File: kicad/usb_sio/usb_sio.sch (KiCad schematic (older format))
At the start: 3 parts

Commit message: Update nrc2016 schema and PCB to use new library symbols
I've added proper schematic symbols for the pre-defined bus sockets to
stop confusion and error by just using the generic "library" socket
component and then relying on the net names to define the pins. Screwed
me once with the VCC and GND switch around, not going to happen again.
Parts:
- removed P?: CONN_01X40, symbol CONN_01X40
- removed U?: MCP2221A, symbol MCP2221A
- added BUS?: Z80_Bus, symbol Z80_Bus
- added C?: CP, symbol CP
- added C? (x2): C, symbol C
- added JP?: JUMPER3, symbol JUMPER3
- added R?: R, symbol R
- added U?: MCP2200, symbol MCP2200
- added U?: 68B50, symbol 68B50
- added U?: DIP_OSCILLATOR, symbol DIP_OSCILLATOR
- added Y?: Crystal, symbol Crystal
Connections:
- net labels added: A0, A6, A7, D0, D1, D2, D3, D4, D5, D6, D7, RX, TX, WR, ~CLK, ~INT, ~M1, ~WR
- net labels removed: ~RESET
- wire segments 8 -> 70
- no-connect marks 0 -> 21
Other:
- note added: "Oscillator Freq: 1.8432MHz\n\nProvides 115200 and 28800 baud without overclocking 68B50"

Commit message: More moving things around. Added sockets and pins symbols
Makes it easier for DRC and has hints for the right footprints already.
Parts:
- removed P?: CONN_01X02, symbol CONN_01X02
- added CON1: USB, symbol USB
- added P?: IO_BUS_PINS, symbol IO_BUS_PINS
- gave numbers to parts that had none: 10
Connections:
- wire segments 70 -> 67
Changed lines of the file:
@@
 $EndDescr
 $Comp
-L CONN_01X02 P?
-U 1 1 57B19EE3
-P 2450 2550
-F 0 "P?" H 2450 2700 50  0000 C CNN
-F 1 "CONN_01X02" V 2550 2550 50  0000 C CNN
-F 2 "" H 2450 2550 50  0000 C CNN
-F 3 "" H 2450 2550 50  0000 C CNN
-	1    2450 2550
-	-1   0    0    -1
-$EndComp
-$Comp
-L MCP2200 U?
+L MCP2200 U1
 U 1 1 57D39A59
 P 4750 2400
-F 0 "U?" H 4900 2450 60  0000 C CNN
+F 0 "U1" H 4900 2450 60  0000 C CNN
 F 1 "MCP2200" H 5350 2450 60  0000 C CNN
 F 2 "" H 4750 2600 60  0000 C CNN
@@
 	2650 2600 3700 2600
 $Comp
-L CP C?
+L CP C1
 U 1 1 57D39AA5
 P 2800 3150
-F 0 "C?" H 2825 3250 50  0000 L CNN
+F 0 "C1" H 2825 3250 50  0000 L CNN
 F 1 "CP" H 2825 3050 50  0000 L CNN
 F 2 "" H 2838 3000 50  0000 C CNN
@@
 	2800 3300 2800 3400
 $Comp
-L GND #PWR?
+L GND #PWR01
 U 1 1 57D39AF5
 P 2800 3400
-F 0 "#PWR?" H 2800 3150 50  0001 C CNN
+F 0 "#PWR01" H 2800 3150 50  0001 C CNN
 F 1 "GND" H 2800 3250 50  0000 C CNN
 F 2 "" H 2800 3400 50  0000 C CNN
@@
 $EndComp
 $Comp
-L Crystal Y?
+L Crystal Y1
 U 1 1 57D39BB8
 P 3750 4300
-F 0 "Y?" H 3750 4450 50  0000 C CNN
+F 0 "Y1" H 3750 4450 50  0000 C CNN
 F 1 "Crystal" H 3750 4150 50  0000 C CNN
 F 2 "" H 3750 4300 50  0000 C CNN
@@
 	3700 3600 3400 3600
 Wire Wire Line
-	3400 3600 3400 4300
-Wire Wire Line
-	3400 4300 3400 4500
+	3400 3600 3400 4500
 Wire Wire Line
 	3400 4300 3600 4300
@@
 	3900 4300 4100 4300
 Wire Wire Line
-	4100 3950 4100 4300
-Wire Wire Line
-	4100 4300 4100 4450
+	4100 3950 4100 4450
 Wire Wire Line
 	4100 3950 3600 3950
@@
 	3600 3700 3700 3700
 $Comp
-L C C?
+L C C2
 U 1 1 57D39C34
 P 3400 4650
-F 0 "C?" H 3425 4750 50  0000 L CNN
+F 0 "C2" H 3425 4750 50  0000 L CNN
 F 1 "C" H 3425 4550 50  0000 L CNN
 F 2 "" H 3438 4500 50  0000 C CNN
@@
 $EndComp
 $Comp
-L C C?
+L C C3
 U 1 1 57D39C64
 P 4100 4650
-F 0 "C?" H 4125 4750 50  0000 L CNN
+F 0 "C3" H 4125 4750 50  0000 L CNN
 F 1 "C" H 4125 4550 50  0000 L CNN
 F 2 "" H 4138 4500 50  0000 C CNN
@@
 	4100 4800 4100 4900
 $Comp
-L GND #PWR?
+L GND #PWR02
 U 1 1 57D39D01
 P 3400 4900
-F 0 "#PWR?" H 3400 4650 50  0001 C CNN
+F 0 "#PWR02" H 3400 4650 50  0001 C CNN
 F 1 "GND" H 3400 4750 50  0000 C CNN
 F 2 "" H 3400 4900 50  0000 C CNN
@@
 $EndComp
 $Comp
-L GND #PWR?
+L GND #PWR03
 U 1 1 57D39D28
 P 4100 4900
-F 0 "#PWR?" H 4100 4650 50  0001 C CNN
+F 0 "#PWR03" H 4100 4650 50  0001 C CNN
 F 1 "GND" H 4100 4750 50  0000 C CNN
 F 2 "" H 4100 4900 50  0000 C CNN
@@
 $EndComp
 $Comp
-L R R?
+L R R1
 U 1 1 57D39FA2
 P 3400 2050
-F 0 "R?" V 3480 2050 50  0000 C CNN
+F 0 "R1" V 3480 2050 50  0000 C CNN
 F 1 "R" V 3400 2050 50  0000 C CNN
 F 2 "" V 3330 2050 50  0000 C CNN
@@
 	3400 1900 3400 1800
 $Comp
-L VCC #PWR?
+L VCC #PWR04
 U 1 1 57D3A036
 P 3400 1800
-F 0 "#PWR?" H 3400 1650 50  0001 C CNN
+F 0 "#PWR04" H 3400 1650 50  0001 C CNN
 F 1 "VCC" H 3400 1950 50  0000 C CNN
 F 2 "" H 3400 1800 50  0000 C CNN
@@
 $EndComp
 $Comp
-L 68B50 U?
+L 68B50 U2
 U 1 1 57D3A94D
 P 5850 4800
-F 0 "U?" H 5950 6750 60  0000 C CNN
+F 0 "U2" H 5950 6750 60  0000 C CNN
 F 1 "68B50" H 6600 6750 60  0000 C CNN
 F 2 "" H 6150 5400 60  0000 C CNN
@@
 	5400 3800 5650 3800
 $Comp
-L DIP_OSCILLATOR U?
+L DIP_OSCILLATOR U3
 U 1 1 57D3CFC5
 P 4650 5500
-F 0 "U?" H 5000 5450 60  0000 C CNN
+F 0 "U3" H 5000 5450 60  0000 C CNN
 F 1 "DIP_OSCILLATOR" V 4600 5800 60  0000 C CNN
 F 2 "" H 4650 5500 60  0000 C CNN
@@
 	5200 5200 5600 5200
 Wire Wire Line
-	5400 4200 5400 4300
-Wire Wire Line
-	5400 4300 5400 4950
+	5400 4200 5400 4950
 Wire Wire Line
 	5400 4200 5650 4200
@@
 Connection ~ 5400 4300
 $Comp
-L VCC #PWR?
+L VCC #PWR05
 U 1 1 57D3D08C
 P 4850 4650
-F 0 "#PWR?" H 4850 4500 50  0001 C CNN
+F 0 "#PWR05" H 4850 4500 50  0001 C CNN
 F 1 "VCC" H 4850 4800 50  0000 C CNN
 F 2 "" H 4850 4650 50  0000 C CNN
@@
 $EndComp
 $Comp
-L GND #PWR?
+L GND #PWR06
 U 1 1 57D3D0B5
 P 4850 5750
-F 0 "#PWR?" H 4850 5500 50  0001 C CNN
+F 0 "#PWR06" H 4850 5500 50  0001 C CNN
 F 1 "GND" H 4850 5600 50  0000 C CNN
 F 2 "" H 4850 5750 50  0000 C CNN
@@
 	5150 4000 5150 4200
 $Comp
-L GND #PWR?
+L GND #PWR07
 U 1 1 57D3D18D
 P 5150 4200
-F 0 "#PWR?" H 5150 3950 50  0001 C CNN
+F 0 "#PWR07" H 5150 3950 50  0001 C CNN
 F 1 "GND" H 5150 4050 50  0000 C CNN
 F 2 "" H 5150 4200 50  0000 C CNN
@@
 	8500 4150 8600 4050
 Wire Bus Line
-	7350 3100 7350 3200
+	7350 3100 7350 5400
 Wire Bus Line
-	7350 3200 7350 3300
+	8500 5400 7350 5400
 Wire Bus Line
-	7350 3300 7350 3500
-Wire Bus Line
-	7350 3500 7350 3600
-Wire Bus Line
-	7350 3600 7350 3700
-Wire Bus Line
-	7350 3700 7350 3800
-Wire Bus Line
-	7350 3800 7350 3900
-Wire Bus Line
-	7350 3900 7350 4000
-Wire Bus Line
-	7350 4000 7350 4100
-Wire Bus Line
-	7350 4100 7350 4200
-Wire Bus Line
-	7350 4200 7350 4400
-Wire Bus Line
-	7350 4400 7350 4500
-Wire Bus Line
-	7350 4500 7350 4800
-Wire Bus Line
-	7350 4800 7350 5300
-Wire Bus Line
-	7350 5300 7350 5400
-Wire Bus Line
-	7350 5400 8500 5400
-Wire Bus Line
-	8500 5400 8500 4850
-Wire Bus Line
-	8500 4850 8500 4750
-Wire Bus Line
-	8500 4750 8500 4650
-Wire Bus Line
-	8500 4650 8500 4550
-Wire Bus Line
-	8500 4550 8500 4450
-Wire Bus Line
-	8500 4450 8500 4350
-Wire Bus Line
-	8500 4350 8500 4250
-Wire Bus Line
-	8500 4250 8500 4150
-Wire Bus Line
-	8500 4150 8500 3850
-Wire Bus Line
-	8500 3850 8500 3650
-Wire Bus Line
-	8500 3650 8500 3350
-Wire Bus Line
-	8500 3350 8500 3250
-Wire Bus Line
-	8500 3250 8500 2650
-Wire Bus Line
-	8500 2650 8500 2550
+	8500 2550 8500 5400
 Text Label 5600 3500 2    60   ~ 0
 TX
@@
 	9000 3550 8600 3550
 $Comp
-L Z80_Bus BUS?
+L Z80_Bus BUS1
 U 1 1 57D3DBDC
 P 9000 1450
-F 0 "BUS?" H 9350 1400 60  0000 C CNN
+F 0 "BUS1" H 9350 1400 60  0000 C CNN
 F 1 "Z80_Bus" V 9550 1100 60  0000 C CNN
 F 2 "" H 9000 1450 60  0000 C CNN
@@
 NoConn ~ 9000 3850
 $Comp
-L JUMPER3 JP?
+L JUMPER3 JP1
 U 1 1 57D3E690
 P 5850 5200
-F 0 "JP?" H 5900 5100 50  0000 L CNN
+F 0 "JP1" H 5900 5100 50  0000 L CNN
 F 1 "JUMPER3" H 5850 5300 50  0000 C BNN
 F 2 "" H 5850 5200 50  0000 C CNN
@@
 Entry Wire Line
 	7250 5200 7350 5300
+$Comp
+L USB CON1
+U 1 1 57D45376
+P 2450 2100
+F 0 "CON1" H 2600 1850 60  0000 C CNN
+F 1 "USB" H 2750 1650 60  0000 C CNN
+F 2 "" H 2450 2100 60  0000 C CNN
+F 3 "" H 2450 2100 60  0000 C CNN
+	1    2450 2100
+	-1   0    0    -1
+$EndComp
+$Comp
+L IO_BUS_PINS P?
+U 1 1 57D3EBEB
+P 8200 750
+F 0 "P?" H 8300 800 60  0000 C CNN
+F 1 "IO_BUS_PINS" V 8600 350 60  0000 C CNN
+F 2 "" H 8200 850 60  0000 C CNN
+F 3 "" H 8200 850 60  0000 C CNN
+	1    8200 750
+	1    0    0    -1
+$EndComp
 $EndSCHEMATC

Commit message: Added schematic for a nrc2016 USB upgrade board for 68B50
This could be an upgrade board for owners of an rc2014 and reuse their
existing 68B50. It uses the IOSEL lines and also puts an appropriate
oscillator so the 68B50 isn't overclocked to heck.

Also uses a MCP2200 USB to serial converter that does hardware flow
control and will have available GPIO for remote I/O using the Microchip
library (remote reset?).

I've made it so the 68B50 oscillator is optional and can continue to run
from the CPU clk.
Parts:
- removed BUS1: Z80_Bus, symbol Z80_Bus
- removed P?: IO_BUS_PINS, symbol IO_BUS_PINS
- added P?: Z80_BUS_PINS, symbol Z80_BUS_PINS
- added P?: IO_BUS_PINS, symbol IO_BUS_PINS
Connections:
- net labels added: IOSEL
- net labels removed: A6, A7
- wire segments 67 -> 69
- no-connect marks 21 -> 32
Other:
- note added: "NEED AN INVERTER HERE... :/"
- moved on the sheet: C1, C2, C3, CON1, JP1, R1, U1, U2, U3, Y1

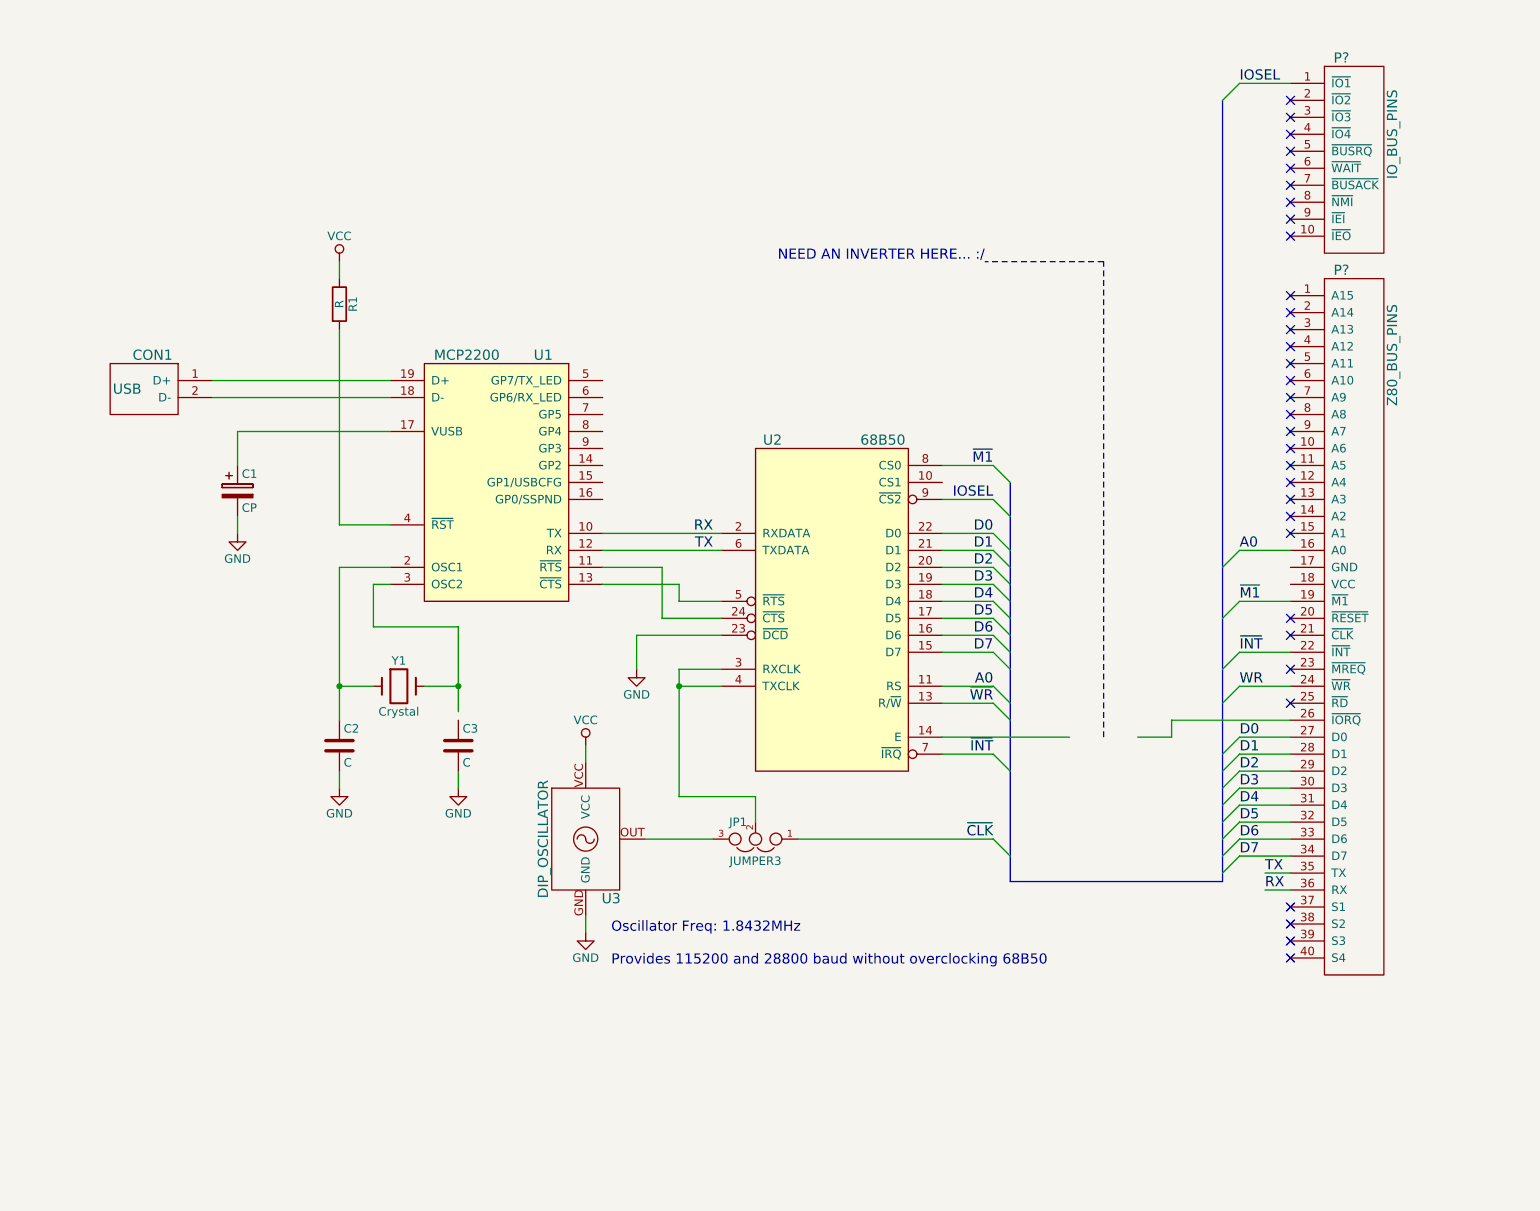
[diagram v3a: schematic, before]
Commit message: Added LEDs and an inverter to the SIO board
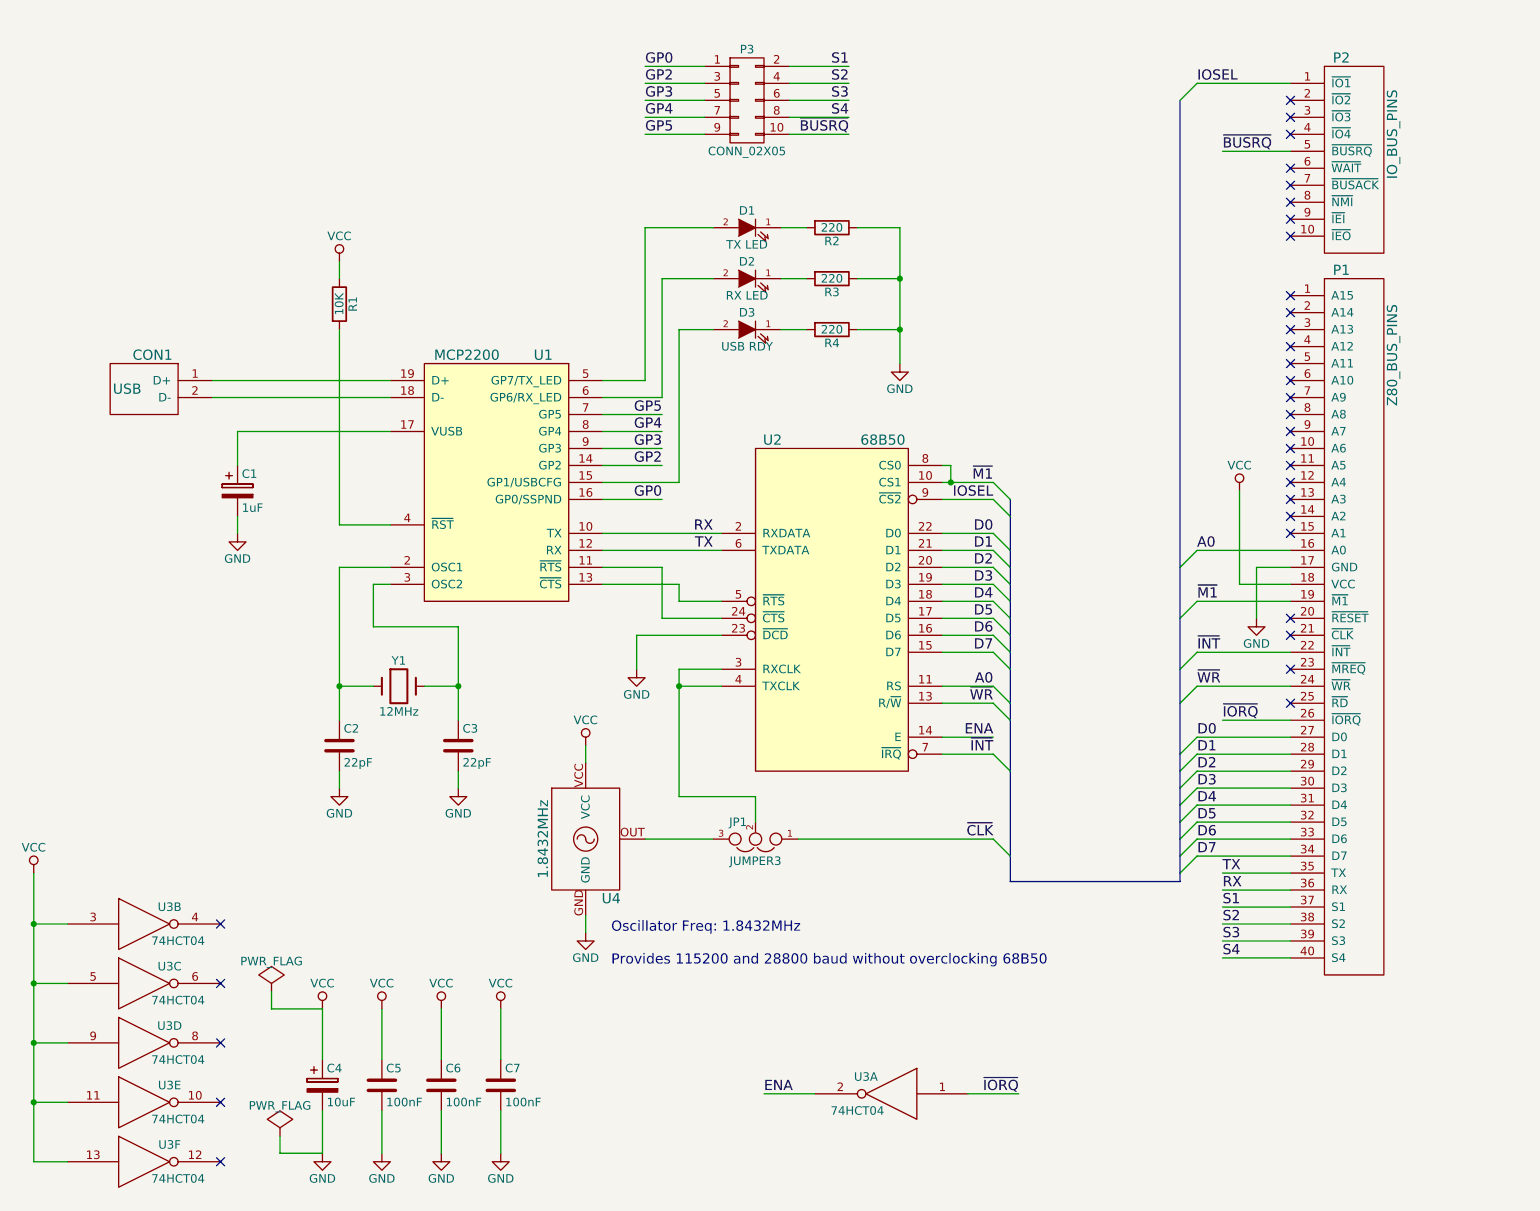
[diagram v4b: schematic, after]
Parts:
- added C4: 10uF, symbol CP
- added C5, C6, C7: 100nF, symbol C
- added D1: TX LED, symbol LED
- added D2: RX LED, symbol LED
- added D3: USB RDY, symbol LED
- added P3: CONN_02X05, symbol CONN_02X05
- added R2, R3, R4: 220, symbol R
- added U3: 74HCT04, symbol 74HCT04
- C1: value CP -> 1uF
- C2, C3: value C -> 22pF
- R1: value R -> 10K
- U4: renamed from U3; value DIP_OSCILLATOR -> 1.8432MHz
- Y1: value Crystal -> 12MHz
- gave numbers to parts that had none: 2
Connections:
- net labels added: ENA, GP0, GP2, GP3, GP4, GP5, S1, S2, S3, S4, ~BUSRQ, ~IORQ
- net labels removed: WR
- wire segments 69 -> 140
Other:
- note removed: "NEED AN INVERTER HERE... :/"
